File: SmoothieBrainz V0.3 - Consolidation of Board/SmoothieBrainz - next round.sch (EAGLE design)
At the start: 219 parts, among them IC1 LPC1769, IC5 LD117ADT33TR, Q1 BSL207SP, Q2 12MHz, SW1 SW_TACT_4P_B, SW3 SW_TACT_4P_B, T1 BC817, U3 USD-SOCKETUSD, X1 MSTBA2, X14 USBPTH, X2 GMSTBA2, X3 GMSTBA4, X4 1751248, X5 1751248, X6 1751248, X7 1751248

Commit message: more routing, almost done
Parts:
- added SJ26: (no value), SparkFun:SOLDERJUMPER_2WAYS
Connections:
- new net V-ENDSTOP: SJ26.2, XMN.1, XMX.1, YMN.1, YMX.1, ZMN.1, ZMX.1
- net 24V: now also SJ26.3
- net 5V: now also SJ26.1; no longer XMN.1, XMX.1, YMN.1, YMX.1, ZMN.1, ZMX.1
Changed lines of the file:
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@@
 <part name="R55" library="resistor" deviceset="R-EU_" device="R0603" value="100k"/>
 <part name="R56" library="varistor" deviceset="VARISTOR" device="CN0603" value="THERM"/>
+<part name="SJ26" library="SparkFun" deviceset="SOLDERJUMPER_2WAY" device="S"/>
 </parts>
 <sheets>
@@
 <instance part="R55" gate="G$1" x="510.54" y="129.54" rot="R180"/>
 <instance part="R56" gate="G$1" x="157.48" y="353.06"/>
+<instance part="SJ26" gate="G$1" x="266.7" y="276.86" rot="R90"/>
 </instances>
 <busses>
@@
 </segment>
 <segment>
-<pinref part="ZMX" gate="G$1" pin="1"/>
-<wire x1="208.28" y1="327.66" x2="218.44" y2="327.66" width="0.1524" layer="91"/>
-<label x="210.82" y="327.66" size="1.778" layer="95"/>
-</segment>
-<segment>
-<pinref part="ZMN" gate="G$1" pin="1"/>
-<wire x1="208.28" y1="312.42" x2="218.44" y2="312.42" width="0.1524" layer="91"/>
-<label x="210.82" y="312.42" size="1.778" layer="95"/>
-</segment>
-<segment>
-<pinref part="YMX" gate="G$1" pin="1"/>
-<wire x1="208.28" y1="297.18" x2="218.44" y2="297.18" width="0.1524" layer="91"/>
-<label x="210.82" y="297.18" size="1.778" layer="95"/>
-</segment>
-<segment>
-<pinref part="YMN" gate="G$1" pin="1"/>
-<wire x1="208.28" y1="281.94" x2="218.44" y2="281.94" width="0.1524" layer="91"/>
-<label x="210.82" y="281.94" size="1.778" layer="95"/>
-</segment>
-<segment>
-<pinref part="XMX" gate="G$1" pin="1"/>
-<wire x1="208.28" y1="266.7" x2="218.44" y2="266.7" width="0.1524" layer="91"/>
-<label x="210.82" y="266.7" size="1.778" layer="95"/>
-</segment>
-<segment>
-<pinref part="XMN" gate="G$1" pin="1"/>
-<wire x1="208.28" y1="251.46" x2="218.44" y2="251.46" width="0.1524" layer="91"/>
-<label x="210.82" y="251.46" size="1.778" layer="95"/>
-</segment>
-<segment>
 <pinref part="U1" gate="G$1" pin="IN"/>
 <wire x1="35.56" y1="-17.78" x2="25.4" y2="-17.78" width="0.1524" layer="91"/>
@@
 <label x="525.78" y="144.78" size="1.778" layer="95"/>
 </segment>
+<segment>
+<pinref part="SJ26" gate="G$1" pin="1"/>
+<wire x1="261.62" y1="276.86" x2="246.38" y2="276.86" width="0.1524" layer="91"/>
+<label x="246.38" y="276.86" size="1.778" layer="95"/>
+</segment>
 </net>
 <net name="N$51" class="0">
@@
 <label x="525.78" y="152.4" size="1.778" layer="95"/>
 </segment>
+<segment>
+<pinref part="SJ26" gate="G$1" pin="3"/>
+<wire x1="271.78" y1="276.86" x2="289.56" y2="276.86" width="0.1524" layer="91"/>
+<label x="284.48" y="276.86" size="1.778" layer="95"/>
+</segment>
 </net>
 <net name="N$16" class="0">
@@
 </segment>
 </net>
+<net name="V-ENDSTOP" class="0">
+<segment>
+<pinref part="ZMX" gate="G$1" pin="1"/>
+<wire x1="208.28" y1="327.66" x2="218.44" y2="327.66" width="0.1524" layer="91"/>
+<label x="210.82" y="327.66" size="1.778" layer="95"/>
+</segment>
+<segment>
+<pinref part="ZMN" gate="G$1" pin="1"/>
+<wire x1="208.28" y1="312.42" x2="218.44" y2="312.42" width="0.1524" layer="91"/>
+<label x="210.82" y="312.42" size="1.778" layer="95"/>
+</segment>
+<segment>
+<pinref part="YMX" gate="G$1" pin="1"/>
+<wire x1="208.28" y1="297.18" x2="218.44" y2="297.18" width="0.1524" layer="91"/>
+<label x="210.82" y="297.18" size="1.778" layer="95"/>
+</segment>
+<segment>
+<pinref part="YMN" gate="G$1" pin="1"/>
+<wire x1="208.28" y1="281.94" x2="218.44" y2="281.94" width="0.1524" layer="91"/>
+<label x="210.82" y="281.94" size="1.778" layer="95"/>
+</segment>
+<segment>
+<pinref part="XMX" gate="G$1" pin="1"/>
+<wire x1="208.28" y1="266.7" x2="218.44" y2="266.7" width="0.1524" layer="91"/>
+<label x="210.82" y="266.7" size="1.778" layer="95"/>
+</segment>
+<segment>
+<pinref part="XMN" gate="G$1" pin="1"/>
+<wire x1="208.28" y1="251.46" x2="218.44" y2="251.46" width="0.1524" layer="91"/>
+<label x="210.82" y="251.46" size="1.778" layer="95"/>
+</segment>
+<segment>
+<pinref part="SJ26" gate="G$1" pin="2"/>
+<wire x1="266.7" y1="271.78" x2="266.7" y2="256.54" width="0.1524" layer="91"/>
+<label x="266.7" y="256.54" size="1.778" layer="95" rot="R90"/>
+</segment>
+</net>

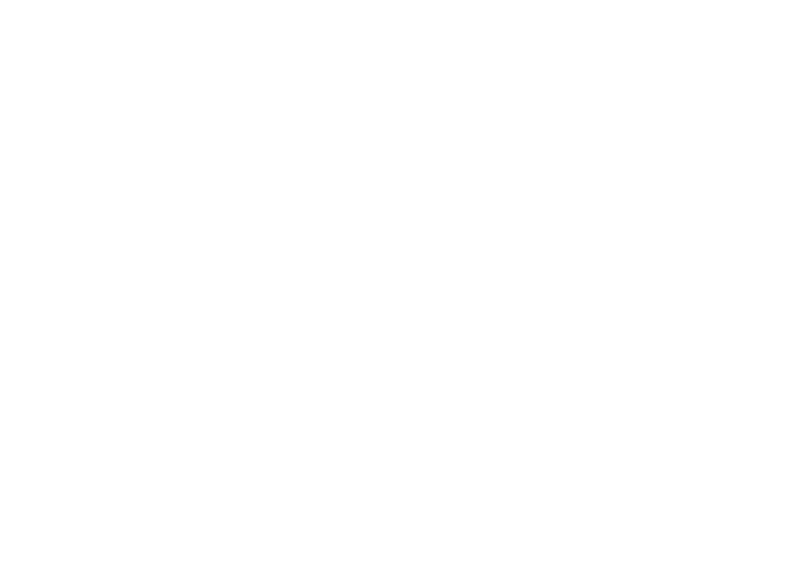
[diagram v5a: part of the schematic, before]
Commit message: Servo connector added!
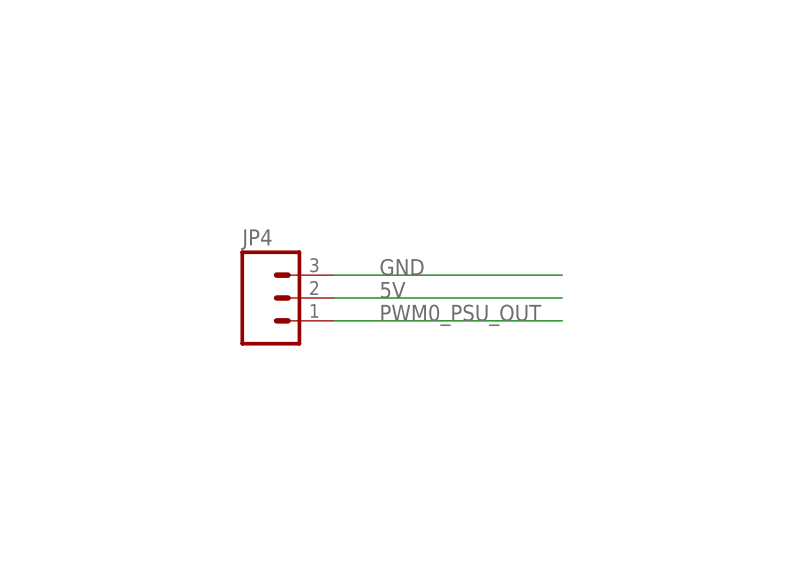
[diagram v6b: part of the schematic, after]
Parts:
- added JP4: (no value), SparkFun-Connectors:M03LOCK
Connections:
- net 5V: now also JP4.2
- net GND: now also JP4.3
- net PWM0_PSU_OUT: now also JP4.1
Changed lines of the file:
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@@
 <part name="R56" library="varistor" deviceset="VARISTOR" device="CN0603" value="THERM"/>
 <part name="SJ26" library="SparkFun" deviceset="SOLDERJUMPER_2WAY" device="S"/>
+<part name="JP4" library="SparkFun-Connectors" deviceset="M03" device="LOCK"/>
 </parts>
 <sheets>
@@
 <instance part="R56" gate="G$1" x="157.48" y="353.06"/>
 <instance part="SJ26" gate="G$1" x="266.7" y="276.86" rot="R90"/>
+<instance part="JP4" gate="G$1" x="251.46" y="-10.16"/>
 </instances>
 <busses>
@@
 <junction x="518.16" y="129.54"/>
 </segment>
+<segment>
+<pinref part="JP4" gate="G$1" pin="3"/>
+<wire x1="259.08" y1="-7.62" x2="284.48" y2="-7.62" width="0.1524" layer="91"/>
+<label x="264.16" y="-7.62" size="1.778" layer="95"/>
+</segment>
 </net>
 <net name="3.3V" class="0">
@@
 <wire x1="78.74" y1="441.96" x2="106.68" y2="441.96" width="0.1524" layer="91"/>
 </segment>
+<segment>
+<pinref part="JP4" gate="G$1" pin="1"/>
+<wire x1="259.08" y1="-12.7" x2="284.48" y2="-12.7" width="0.1524" layer="91"/>
+<label x="264.16" y="-12.7" size="1.778" layer="95"/>
+</segment>
 </net>
 <net name="PWM1_BED_HEATER" class="0">
@@
 <label x="246.38" y="276.86" size="1.778" layer="95"/>
 </segment>
-</net>
+<segment>
+<pinref part="JP4" gate="G$1" pin="2"/>
+<wire x1="259.08" y1="-10.16" x2="284.48" y2="-10.16" width="0.1524" layer="91"/>
+<label x="264.16" y="-10.16" size="1.778" layer="95"/>
+</segment>
+</net>

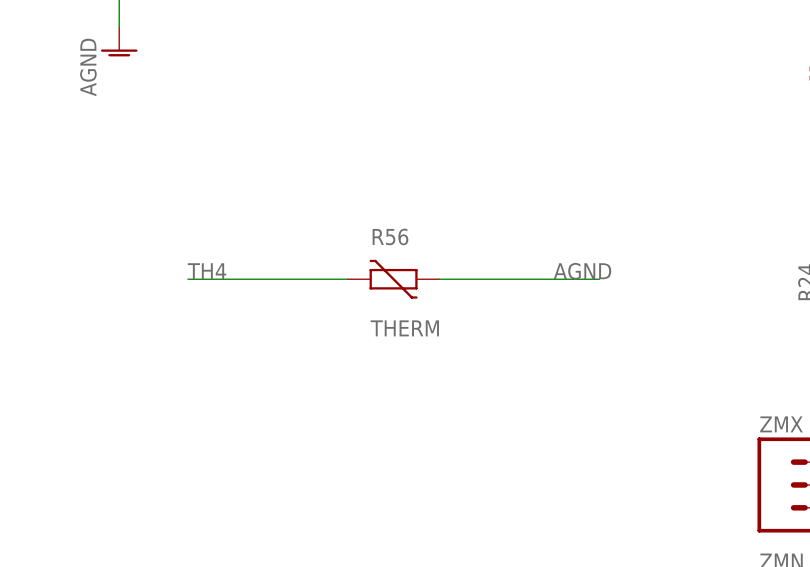
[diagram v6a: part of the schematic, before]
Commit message: added solder jumper to pcb thermistor circuit
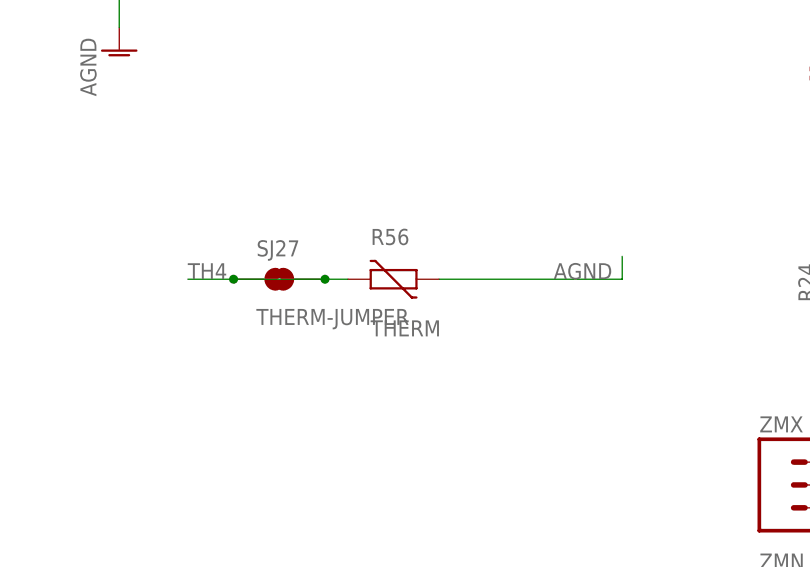
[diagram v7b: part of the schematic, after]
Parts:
- added SJ27: THERM-JUMPER, SparkFun-Retired:SOLDERJUMPERTRACE
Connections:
- net TH4: now also SJ27.1, SJ27.2
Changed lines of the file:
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@@
 <part name="SJ26" library="SparkFun" deviceset="SOLDERJUMPER_2WAY" device="S"/>
 <part name="JP4" library="SparkFun-Connectors" deviceset="M03" device="LOCK"/>
+<part name="SJ27" library="SparkFun-Retired" deviceset="SOLDERJUMPER" device="TRACE" value="THERM-JUMPER"/>
 </parts>
 <sheets>
@@
 <instance part="SJ26" gate="G$1" x="266.7" y="276.86" rot="R90"/>
 <instance part="JP4" gate="G$1" x="251.46" y="-10.16"/>
+<instance part="SJ27" gate="1" x="144.78" y="353.06"/>
 </instances>
 <busses>
@@
 <segment>
 <pinref part="R56" gate="G$1" pin="2"/>
-<wire x1="152.4" y1="353.06" x2="134.62" y2="353.06" width="0.1524" layer="91"/>
+<wire x1="152.4" y1="353.06" x2="149.86" y2="353.06" width="0.1524" layer="91"/>
 <label x="134.62" y="353.06" size="1.778" layer="95"/>
+<pinref part="SJ27" gate="1" pin="2"/>
+<wire x1="149.86" y1="353.06" x2="139.7" y2="353.06" width="0.1524" layer="91"/>
+<junction x="149.86" y="353.06"/>
+<pinref part="SJ27" gate="1" pin="1"/>
+<wire x1="139.7" y1="353.06" x2="134.62" y2="353.06" width="0.1524" layer="91"/>
+<junction x="139.7" y="353.06"/>
 </segment>
 </net>
@@
 </segment>
 <segment>
+<label x="175.26" y="353.06" size="1.778" layer="95"/>
+<wire x1="182.88" y1="353.06" x2="182.88" y2="355.6" width="0.1524" layer="91"/>
 <pinref part="R56" gate="G$1" pin="1"/>
-<wire x1="162.56" y1="353.06" x2="180.34" y2="353.06" width="0.1524" layer="91"/>
-<label x="175.26" y="353.06" size="1.778" layer="95"/>
-</segment>
-</net>
+<wire x1="162.56" y1="353.06" x2="182.88" y2="353.06" width="0.1524" layer="91"/>
+</segment>
+</net>
